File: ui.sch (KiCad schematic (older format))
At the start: 0 parts

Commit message: Made a overview on the toplevel schematic and added the SRAM subschematic.
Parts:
- added U1: ICE40HX4K-TQ144, symbol ice40hx4k:ICE40HX4K-TQ144
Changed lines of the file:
@@
 EESchema Schematic File Version 4
+LIBS:ice40_breakout-cache
 EELAYER 29 0
 EELAYER END
 $Descr A4 11693 8268
 encoding utf-8
-Sheet 3 5
+Sheet 3 6
 Title ""
 Date ""
@@
 Comment4 ""
 $EndDescr
+$Comp
+L ice40hx4k:ICE40HX4K-TQ144 U1
+U 2 1 5CAB837C
+P 7150 3075
+F 0 "U1" H 8128 3274 50  0000 L CNN
+F 1 "ICE40HX4K-TQ144" H 8128 3183 50  0000 L CNN
+F 2 "" H 7150 3075 50  0001 C CNN
+F 3 "" H 7150 3075 50  0001 C CNN
+	2    7150 3075
+	1    0    0    -1
+$EndComp
 $EndSCHEMATC

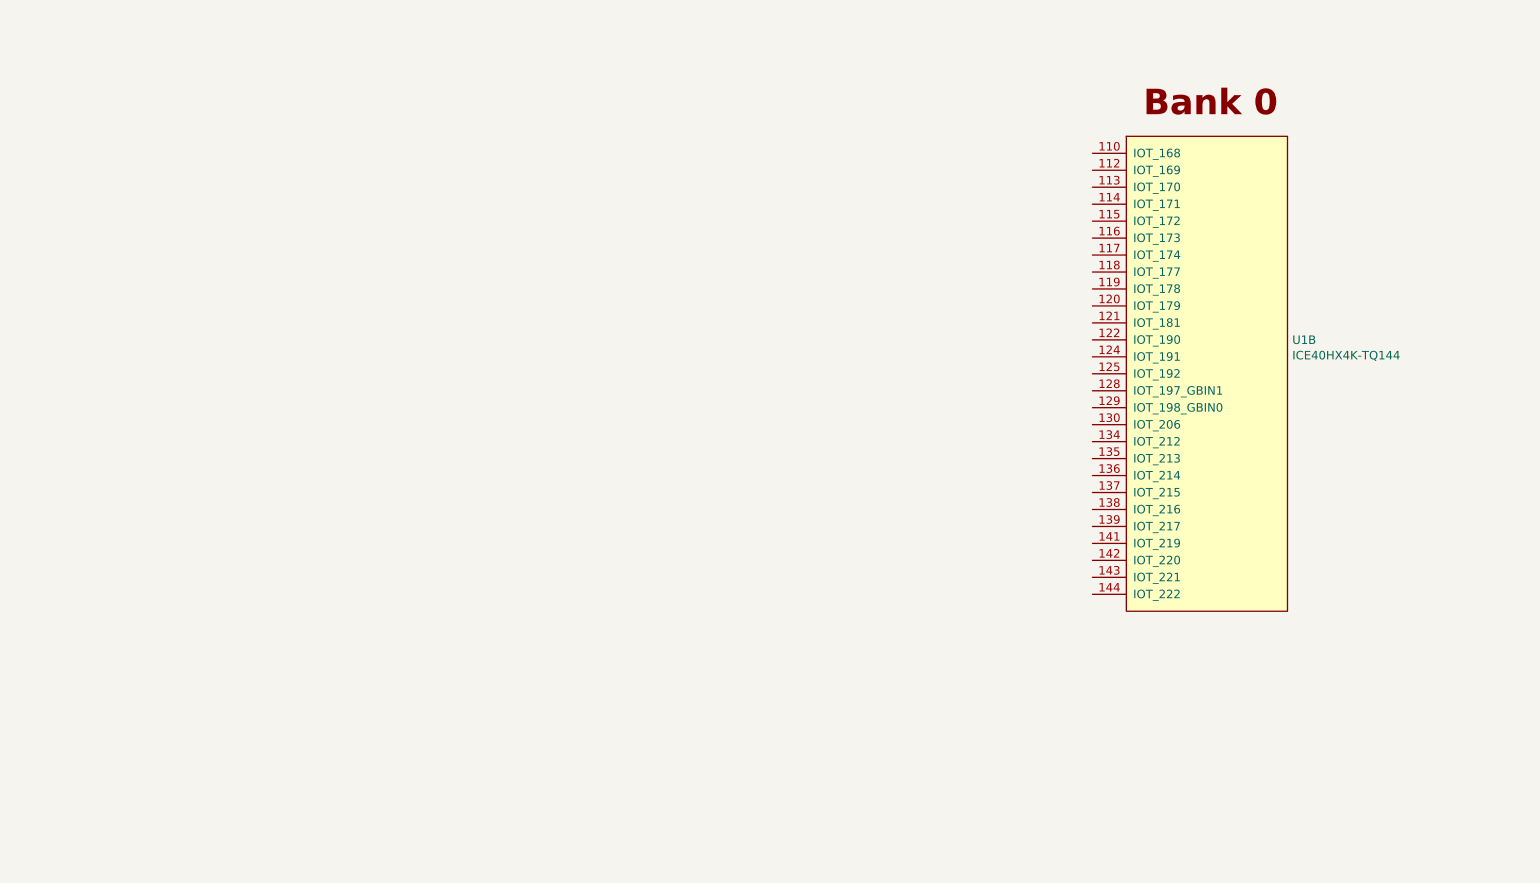
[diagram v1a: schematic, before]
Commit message: sram, ui, power, flash and header
SRAM: mostly done. Changed the choosen IC to a faster one in a differenc housing.

POWER: added some step down converter for 3.3 V and 1.2 V. The 1.2 V is oversized and could be changed to a smaller one

Programmer: added flash.

HEADER: Added Arduino Uno like headers with 5 V signal level. Analog is not connected now, will get an I2C ADC in future. Also added 3 digilent pmod styled connector with 3.3 V signal level.

UI: added 5 buttons and 8 LEDs. There is some space left over, maybe double the LED count in future.
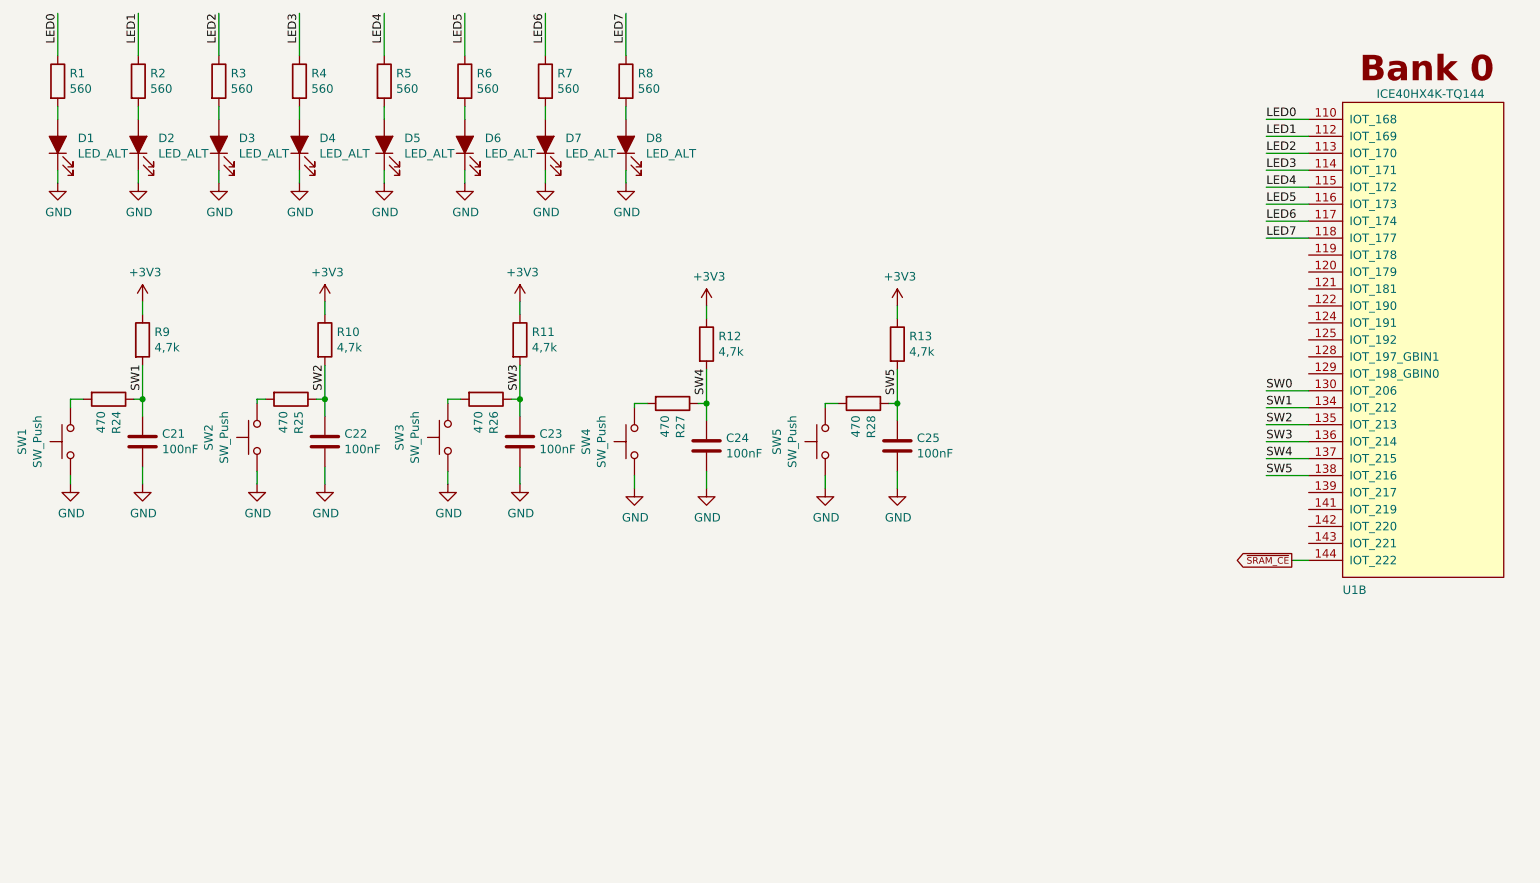
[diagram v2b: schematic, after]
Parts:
- added C21, C22, C23, C24, C25: 100nF, Capacitor_SMD:C_0603_1608Metric, symbol Device:C
- added D1, D2, D3, D4, D5, D6, D7, D8: LED_ALT, LED_SMD:LED_0603_1608Metric, symbol Device:LED_ALT
- added R1, R2, R3, R4, R5, R6, R7, R8: 560, Resistor_SMD:R_0603_1608Metric, symbol Device:R
- added R10, R11, R12, R13, R9: 4,7k, Resistor_SMD:R_0603_1608Metric, symbol Device:R
- added R24, R25, R26, R27, R28: 470, Resistor_SMD:R_0603_1608Metric, symbol Device:R
- added SW1, SW2, SW3, SW4, SW5: SW_Push, footprints:SW_SPST_TL3305A, symbol Switch:SW_Push
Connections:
- net LED0: now reaches U1.110 (IOT_168)
- net LED0: now also R1.1
- net LED1: now reaches U1.112 (IOT_169)
- net LED1: now also R2.1
- net LED2: now reaches U1.113 (IOT_170)
- net LED2: now also R3.1
- net LED3: now reaches U1.114 (IOT_171)
- net LED3: now also R4.1
- net LED4: now reaches U1.115 (IOT_172)
- net LED4: now also R5.1
- net LED5: now reaches U1.116 (IOT_173)
- net LED5: now also R6.1
- net LED6: now reaches U1.117 (IOT_174)
- net LED6: now also R7.1
- net LED7: now reaches U1.118 (IOT_177)
- net LED7: now also R8.1
- net SW0: now reaches U1.130 (IOT_206)
- net SW1: now reaches U1.134 (IOT_212)
- net SW1: now also C21.1, R24.1, R9.2
- net SW2: now reaches U1.135 (IOT_213)
- net SW2: now also C22.1, R10.2, R25.1
- net SW3: now reaches U1.136 (IOT_214)
- net SW3: now also C23.1, R11.2, R26.1
- net SW4: now reaches U1.137 (IOT_215)
- net SW4: now also C24.1, R12.2, R27.1
- net SW5: now reaches U1.138 (IOT_216)
- net SW5: now also C25.1, R13.2, R28.1
- net ~SRAM_CE~: now reaches U1.144 (IOT_222)
- new net: R24.2, SW1.2
- new net: R25.2, SW2.2
- new net: R26.2, SW3.2
- new net: R27.2, SW4.2
- new net: R28.2, SW5.2
- new net: D1.2 (A), R1.2
- new net: D2.2 (A), R2.2
- new net: D3.2 (A), R3.2
- new net: D4.2 (A), R4.2
- new net: D5.2 (A), R5.2
- new net: D6.2 (A), R6.2
- new net: D7.2 (A), R7.2
- new net: D8.2 (A), R8.2
- new net +3V3: R10.1, R11.1, R12.1, R13.1, R9.1
- new net GND: C21.2, C22.2, C23.2, C24.2, C25.2, D1.1 (K), D2.1 (K), D3.1 (K), D4.1 (K), D5.1 (K), D6.1 (K), D7.1 (K), D8.1 (K), SW1.1, SW2.1, SW3.1, SW4.1, SW5.1
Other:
- moved on the sheet: U1B

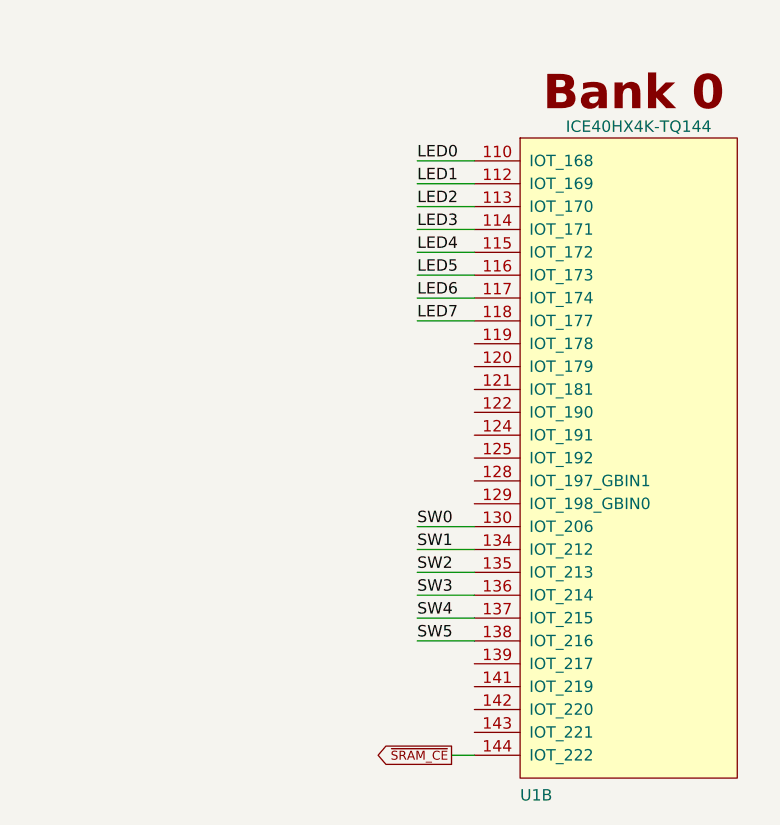
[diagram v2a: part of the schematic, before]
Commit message: Continued on Programmer, moved the header signals around the package to free some space for a fully featured UART/RS232(TTL)
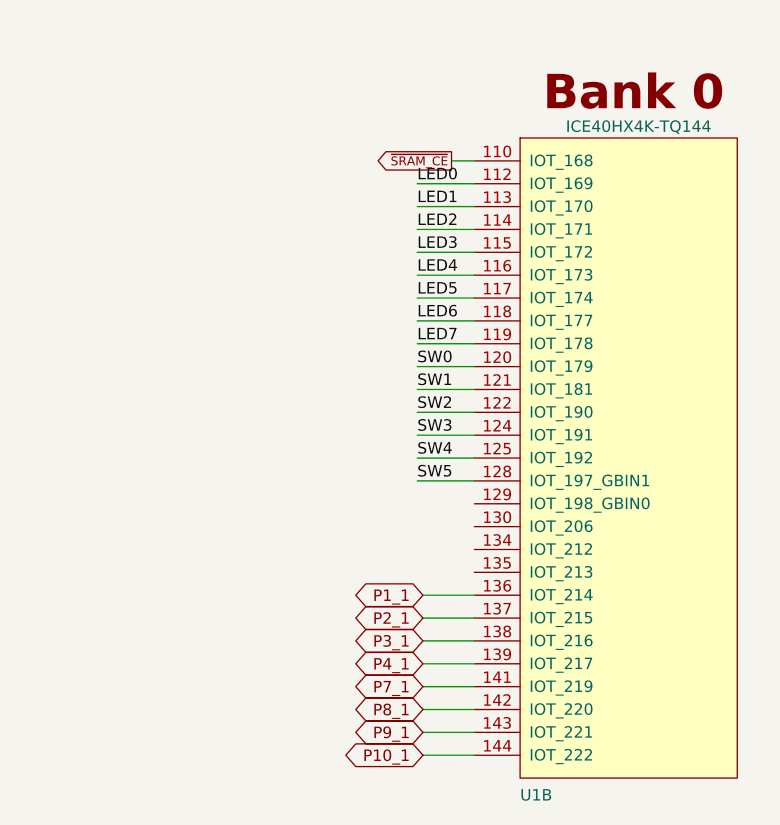
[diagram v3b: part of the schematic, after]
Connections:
- net LED0: now also U1.112 (IOT_169); no longer U1.110 (IOT_168)
- net LED1: now also U1.113 (IOT_170); no longer U1.112 (IOT_169)
- net LED2: now also U1.114 (IOT_171); no longer U1.113 (IOT_170)
- net LED3: now also U1.115 (IOT_172); no longer U1.114 (IOT_171)
- net LED4: now also U1.116 (IOT_173); no longer U1.115 (IOT_172)
- net LED5: now also U1.117 (IOT_174); no longer U1.116 (IOT_173)
- net LED6: now also U1.118 (IOT_177); no longer U1.117 (IOT_174)
- net LED7: now also U1.119 (IOT_178); no longer U1.118 (IOT_177)
- net SW0: now also U1.120 (IOT_179); no longer U1.130 (IOT_206)
- net SW1: now also U1.121 (IOT_181); no longer U1.134 (IOT_212)
- net SW2: now also U1.122 (IOT_190); no longer U1.135 (IOT_213)
- net SW3: now also U1.124 (IOT_191); no longer U1.136 (IOT_214)
- net SW4: now also U1.125 (IOT_192); no longer U1.137 (IOT_215)
- net SW5: now also U1.128 (IOT_197_GBIN1); no longer U1.138 (IOT_216)
- net ~SRAM_CE~: now also U1.110 (IOT_168); no longer U1.144 (IOT_222)
- net P4_1: now reaches U1.139 (IOT_217)
- net P7_1: now reaches U1.141 (IOT_219)
- net P8_1: now reaches U1.142 (IOT_220)
- net P9_1: now reaches U1.143 (IOT_221)
- new net P10_1: U1.144 (IOT_222)
- new net P1_1: U1.136 (IOT_214)
- new net P2_1: U1.137 (IOT_215)
- new net P3_1: U1.138 (IOT_216)
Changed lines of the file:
@@
 Wire Wire Line
 	4200 950  4200 1200
-Text Label 7975 1575 0    50   ~ 0
+Text Label 7975 1675 0    50   ~ 0
 LED0
-Wire Wire Line
-	7975 1575 8225 1575
-Text Label 7975 1675 0    50   ~ 0
-LED1
 Wire Wire Line
 	7975 1675 8225 1675
 Text Label 7975 1775 0    50   ~ 0
-LED2
+LED1
 Wire Wire Line
 	7975 1775 8225 1775
 Text Label 7975 1875 0    50   ~ 0
-LED3
+LED2
 Wire Wire Line
 	7975 1875 8225 1875
 Text Label 7975 1975 0    50   ~ 0
-LED4
+LED3
 Wire Wire Line
 	7975 1975 8225 1975
 Text Label 7975 2075 0    50   ~ 0
-LED5
+LED4
 Wire Wire Line
 	7975 2075 8225 2075
 Text Label 7975 2175 0    50   ~ 0
-LED6
+LED5
 Wire Wire Line
 	7975 2175 8225 2175
 Text Label 7975 2275 0    50   ~ 0
+LED6
+Wire Wire Line
+	7975 2275 8225 2275
+Text Label 7975 2375 0    50   ~ 0
 LED7
 Wire Wire Line
-	7975 2275 8225 2275
+	7975 2375 8225 2375
 $Comp
 L power:GND #PWR09
@@
 Text Label 5800 3200 1    50   ~ 0
 SW5
-Text Label 7975 3175 0    50   ~ 0
+Text Label 7975 2475 0    50   ~ 0
 SW0
 Wire Wire Line
-	7975 3175 8225 3175
-Text Label 7975 3275 0    50   ~ 0
+	7975 2475 8225 2475
+Text Label 7975 2575 0    50   ~ 0
 SW1
 Wire Wire Line
-	7975 3275 8225 3275
-Text Label 7975 3375 0    50   ~ 0
+	7975 2575 8225 2575
+Text Label 7975 2675 0    50   ~ 0
 SW2
 Wire Wire Line
-	7975 3375 8225 3375
-Text Label 7975 3475 0    50   ~ 0
+	7975 2675 8225 2675
+Text Label 7975 2775 0    50   ~ 0
 SW3
 Wire Wire Line
-	7975 3475 8225 3475
-Text Label 7975 3575 0    50   ~ 0
+	7975 2775 8225 2775
+Text Label 7975 2875 0    50   ~ 0
 SW4
 Wire Wire Line
-	7975 3575 8225 3575
-Text Label 7975 3675 0    50   ~ 0
+	7975 2875 8225 2875
+Text Label 7975 2975 0    50   ~ 0
 SW5
 Wire Wire Line
-	7975 3675 8225 3675
+	7975 2975 8225 2975
 $Comp
 L power:+3V3 #PWR037
@@
 Wire Wire Line
 	5800 2675 5800 2750
-Text GLabel 8125 4175 0    39   Output ~ 0
+Text GLabel 8125 1575 0    39   Output ~ 0
 ~SRAM_CE~
 Wire Wire Line
-	8125 4175 8225 4175
+	8125 1575 8225 1575
 $Comp
 L Device:C C21
@@
 Wire Wire Line
 	3150 3225 3225 3225
+Wire Wire Line
+	8000 3475 8225 3475
+Wire Wire Line
+	8000 3575 8225 3575
+Wire Wire Line
+	8000 3675 8225 3675
+Wire Wire Line
+	8000 3775 8225 3775
+Wire Wire Line
+	8000 3875 8225 3875
+Wire Wire Line
+	8000 3975 8225 3975
+Wire Wire Line
+	8000 4075 8225 4075
+Wire Wire Line
+	8000 4175 8225 4175
+Text GLabel 8000 3475 0    50   BiDi ~ 0
+P1_1
+Text GLabel 8000 3575 0    50   BiDi ~ 0
+P2_1
+Text GLabel 8000 3675 0    50   BiDi ~ 0
+P3_1
+Text GLabel 8000 3775 0    50   BiDi ~ 0
+P4_1
+Text GLabel 8000 3875 0    50   BiDi ~ 0
+P7_1
+Text GLabel 8000 3975 0    50   BiDi ~ 0
+P8_1
+Text GLabel 8000 4075 0    50   BiDi ~ 0
+P9_1
+Text GLabel 8000 4175 0    50   BiDi ~ 0
+P10_1
 $EndSCHEMATC

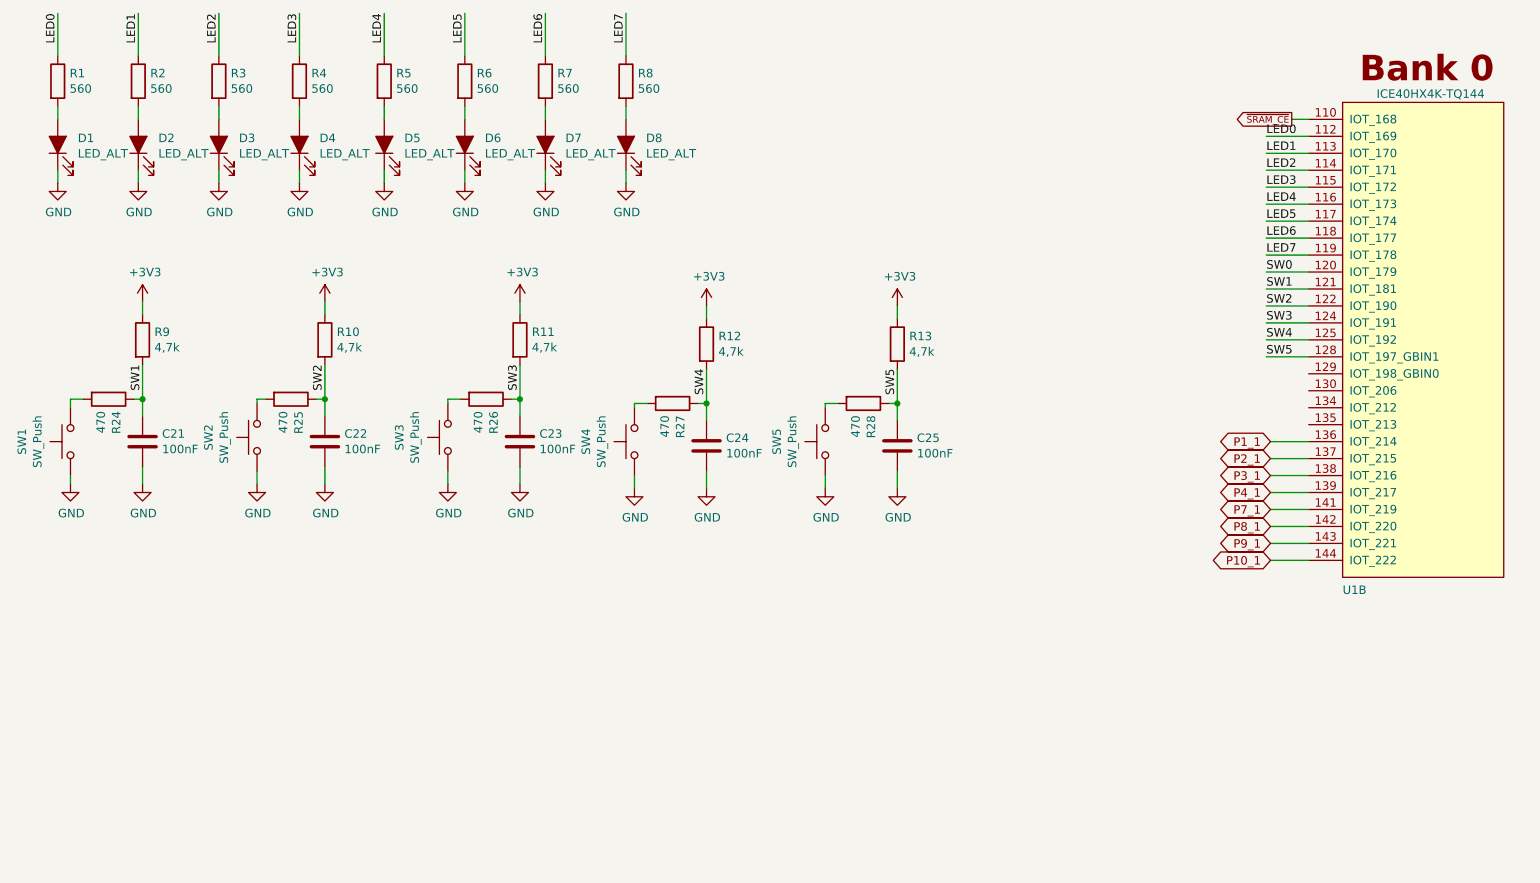
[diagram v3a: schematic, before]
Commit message: Added switches, added 5 V rail and 17 V input(with filtering). Power is mostly done.
Also added a first version of buffers to ftdi chip. I'll change the evtl.

Started to route power section.
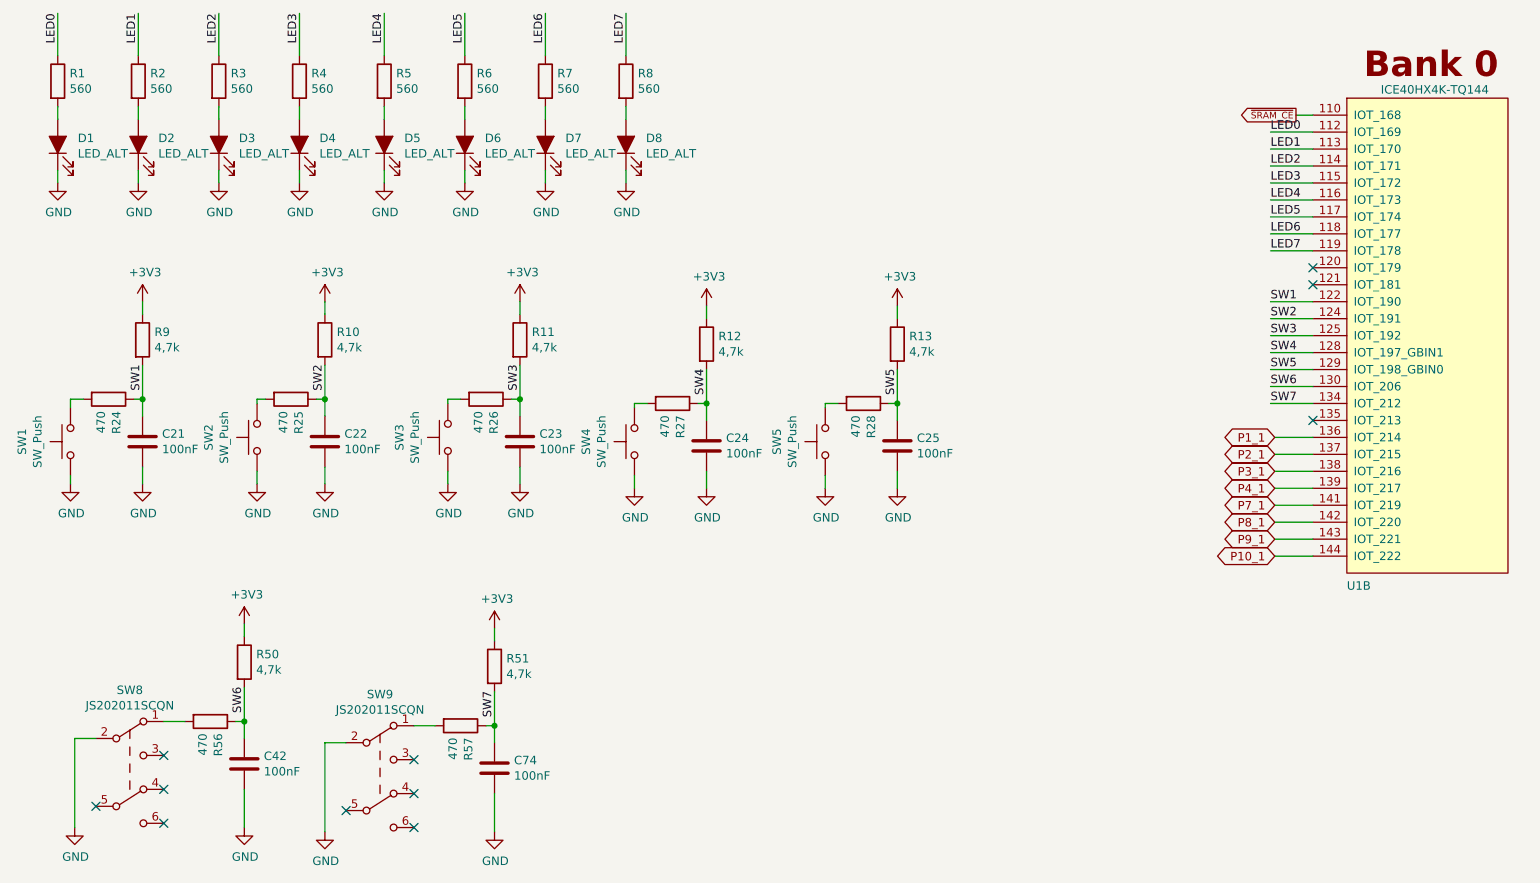
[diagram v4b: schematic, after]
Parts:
- added C42, C74: 100nF, Capacitor_SMD:C_0603_1608Metric, symbol Device:C
- added R50, R51: 4,7k, Resistor_SMD:R_0603_1608Metric, symbol Device:R
- added R56, R57: 470, Resistor_SMD:R_0603_1608Metric, symbol Device:R
- added SW8, SW9: JS202011SCQN, footprints:SW_SLIDE_DPDT_Slide_CK_JS202011SCQN_W3mm_P2.5mm_footprint, symbol sw_dpdt:SW_DPDT
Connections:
- net +3V3: now also R50.1, R51.1
- net GND: now also C42.2, C74.2, SW8.2 (B), SW9.2 (B)
- net SW1: now also U1.122 (IOT_190); no longer U1.121 (IOT_181)
- net SW2: now also U1.124 (IOT_191); no longer U1.122 (IOT_190)
- net SW3: now also U1.125 (IOT_192); no longer U1.124 (IOT_191)
- net SW4: now also U1.128 (IOT_197_GBIN1); no longer U1.125 (IOT_192)
- net SW5: now also U1.129 (IOT_198_GBIN0); no longer U1.128 (IOT_197_GBIN1)
- net SW6: now reaches U1.130 (IOT_206)
- net SW6: now also C42.1, R50.2, R56.1
- net SW7: now reaches U1.134 (IOT_212)
- net SW7: now also C74.1, R51.2, R57.1
- net SW0: no longer names the net of U1.120 (IOT_179)
- new net: R56.2, SW8.1 (A)
- new net: R57.2, SW9.1 (A)
- no-connect marks 0 -> 11
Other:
- moved on the sheet: U1B
